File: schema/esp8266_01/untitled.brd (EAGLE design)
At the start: 37.1 x 41.3 mm, 24 parts, among them IC1 LD117AS33TR, J1 DCJ0202, Q1 BC857ASMD, X2 12 MHz

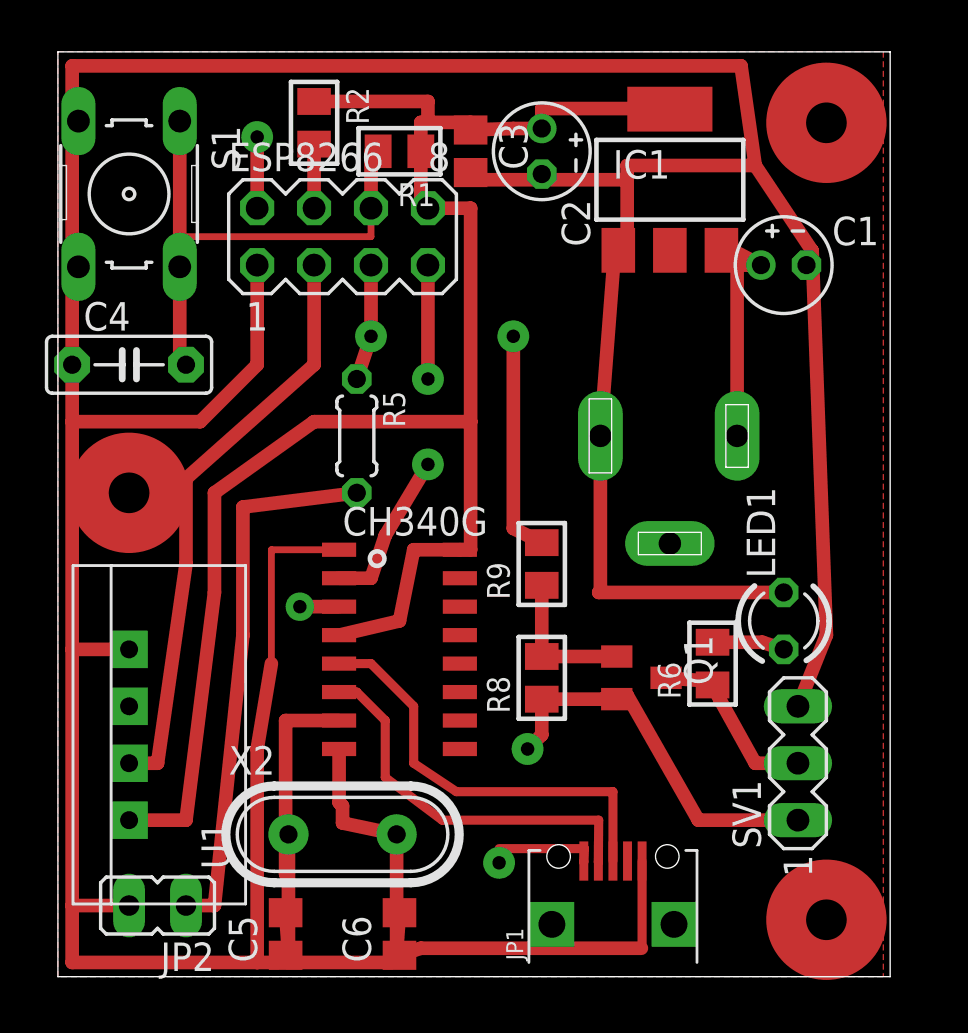
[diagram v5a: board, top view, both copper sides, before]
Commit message: Fixed all schemas. Just needed to change miscro USB sockets
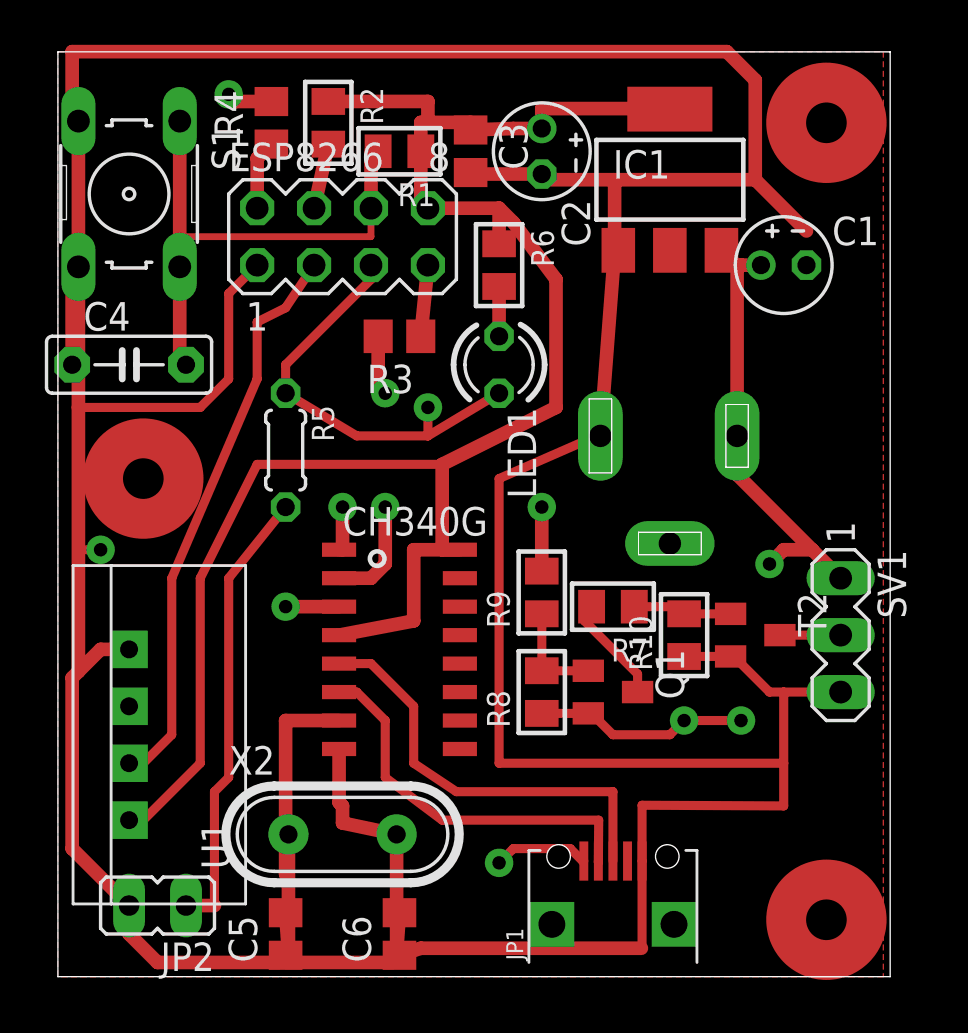
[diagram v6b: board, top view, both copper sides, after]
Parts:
- added R10, R7: 4.7K, rc-master:R0805
- added R3: 1.5K, resistor:R0805
- added R4: 500, resistor:R0805
- added T2: BC847, transistor:SOT23
- R8: value 1K -> 4.7K
- moved R6 20.2 mm to (37.5, 71.1), turned to 270 degrees
- moved LED1 17.1 mm to (37.5, 66.7), turned to 270 degrees
- moved SV1 6.02 mm to (52.7, 54.6), turned to 270 degrees
- moved R5 3.24 mm to (27.9, 62.9)
- moved Q1 1.42 mm to (42.5, 52.1)
- moved R9 1.27 mm to (39.4, 56.5)
- moved R2 0.63 mm to (29.8, 77.5)
- moved R8 0.63 mm to (39.4, 52.1)
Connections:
- removed net RX: ESP8266.2, U$1.3
- removed net S$1: C1.+, IC1.3, J1.3
- removed net TX: ESP8266.7, U$1.2
- new net N$200: C1.+, IC1.3, J1.3, JP1.1, Q1.E, R8.1, SV1.1
- new net N$36: ESP8266.7, R3.1
- new net N$40: ESP8266.2, R4.1
- new net N$41: R4.2, U$1.3
- new net N$46: R10.2, R7.1, T2.1
- new net N$48: SV1.2, T2.3
- net GND: now also R10.1, T2.2; no longer LED1.K
- net GPIO0: now also LED1.K
- net N$37: now also R3.2, U$1.2; no longer JP1.1, Q1.E, R8.1, SV1.1
- net N$7: now also R7.2; no longer R6.1, SV1.2
- net VCC: now also R6.1
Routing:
- net N$200: track 0.00 -> 34.0 mm
- net TX: track 12.2 -> 0.00 mm, vias 2 -> 0
- net N$37: track 19.2 -> 7.53 mm
- net S$1: track 10.6 -> 0.00 mm
- net GPIO0: track 15.2 -> 22.0 mm, vias 1 -> 0
- net GND: track 211.9 -> 205.4 mm
- net RX: track 4.92 -> 0.00 mm, vias 1 -> 0
- net N$46: track 0.00 -> 4.43 mm
- net N$41: track 0.00 -> 4.42 mm
- net N$1: track 24.2 -> 20.2 mm
- net N$36: track 0.00 -> 3.19 mm
- net N$40: track 0.00 -> 3.12 mm
- net N$7: track 8.03 -> 4.92 mm
- net VCC: track 79.1 -> 82.2 mm
- net N$48: track 0.00 -> 2.71 mm
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
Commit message: Finished ver 1.0 for both boards
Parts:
- C1: value 10uF -> 100nF
- C3: value (none) -> 10uF
- moved C4 0.64 mm to (21.0, 67.3)
- moved S1 0.64 mm to (21.0, 74.9)
- moved R5 0.63 mm to (27.9, 63.5)
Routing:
- net N$1: track 20.2 -> 21.0 mm
- net RESET: track 25.1 -> 25.9 mm
- net GND: track 205.4 -> 206.1 mm
- net N$41: track 4.42 -> 5.06 mm
- net N$200: track 34.0 -> 34.5 mm
